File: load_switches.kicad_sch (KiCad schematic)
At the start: 19 parts, among them U10 TPS22965TDSGRQ1, U11 TPS22965TDSGRQ1, U12 TPS22965TDSGRQ1, U9 TPS22965TDSGRQ1

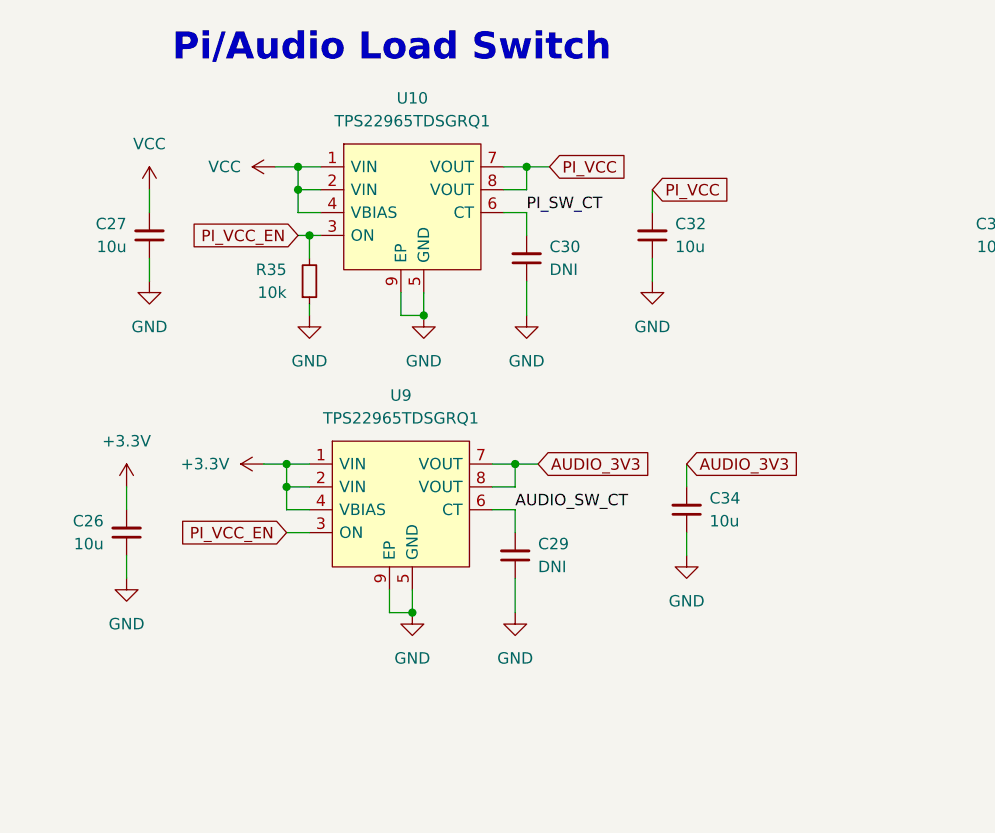
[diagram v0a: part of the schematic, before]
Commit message: schematic: add resistors to allow latching pi power
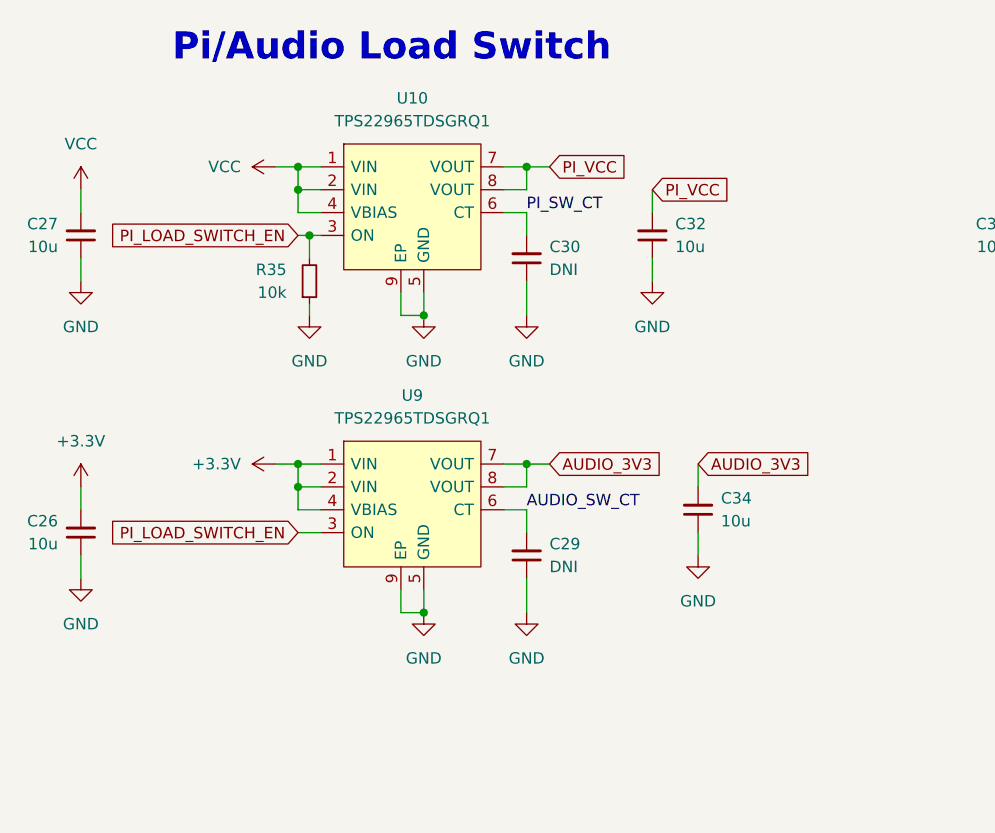
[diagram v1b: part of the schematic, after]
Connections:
- net PI_VCC_EN renamed PI_LOAD_SWITCH_EN
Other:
- moved on the sheet: C26, C27, C29, C34, U9

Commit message: ci: prepare files for CI
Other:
- title: (none) -> piPod IO/SMC Board
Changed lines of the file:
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@@
 (kicad_sch (version 20211123) (generator eeschema)
   (paper "A4")
+  (title_block
+    (title "piPod IO/SMC Board")
+    (date "${DATE}")
+    (rev "%{TAG} (${REVISION})")
+  )
   (junction (at 62.23 55.88) (diameter 0) (color 0 0 0 0)
   )

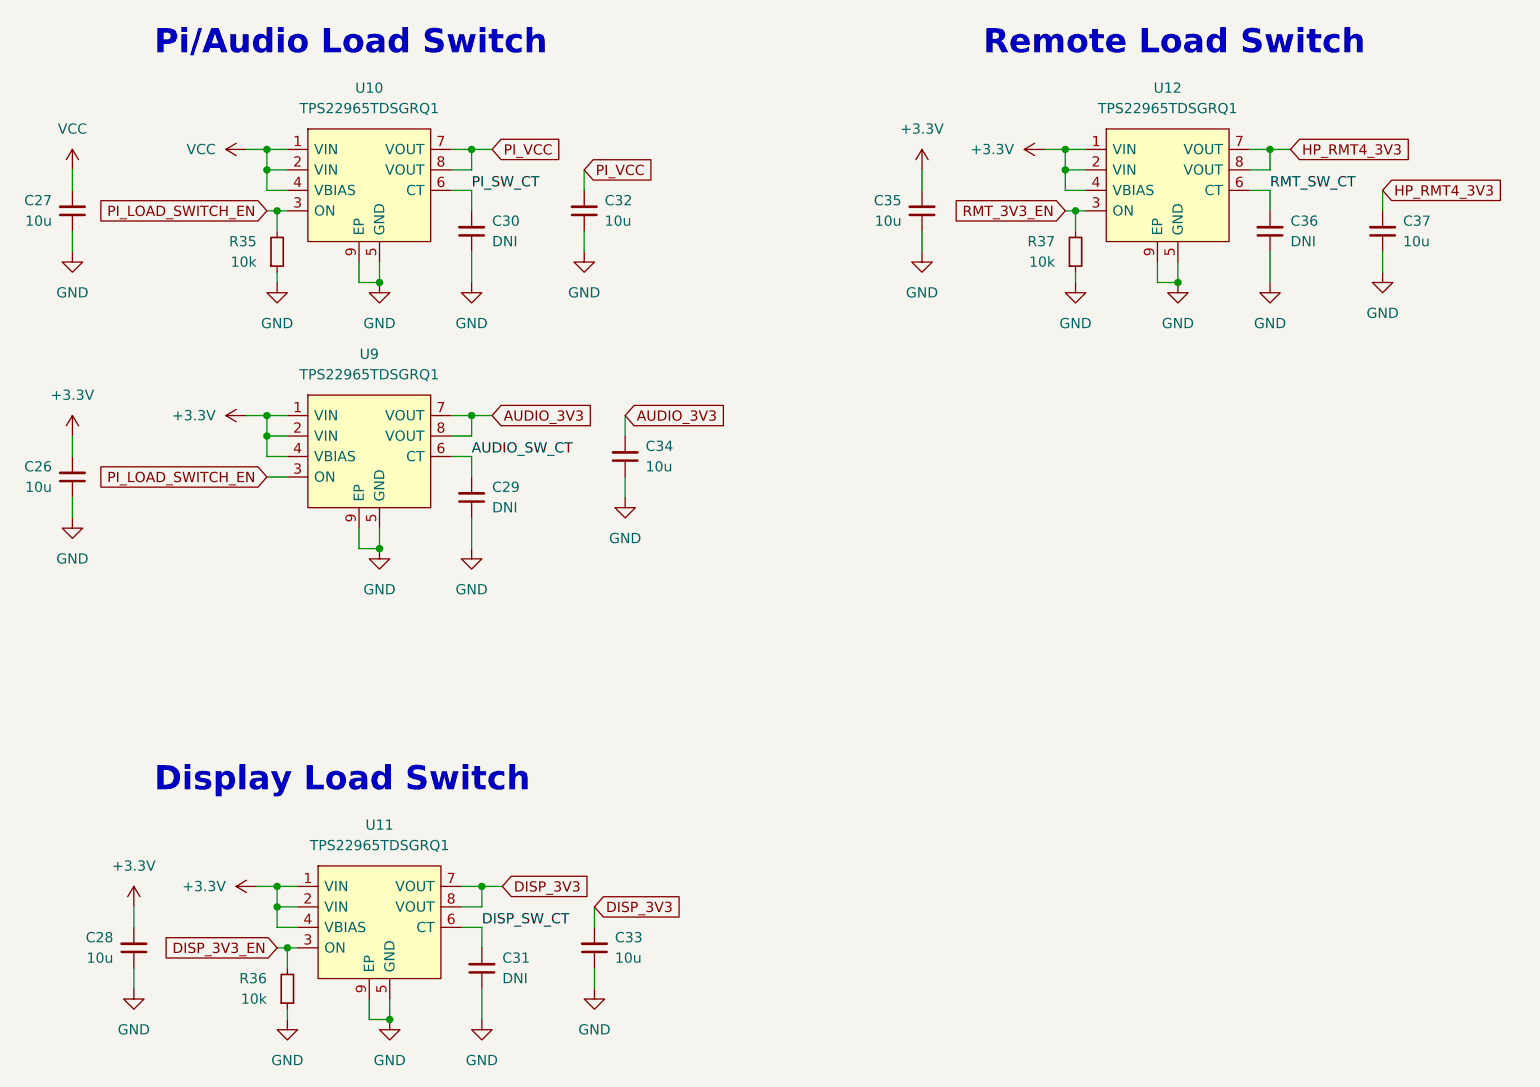
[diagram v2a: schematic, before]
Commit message: ci: test marking parts in sch for bom
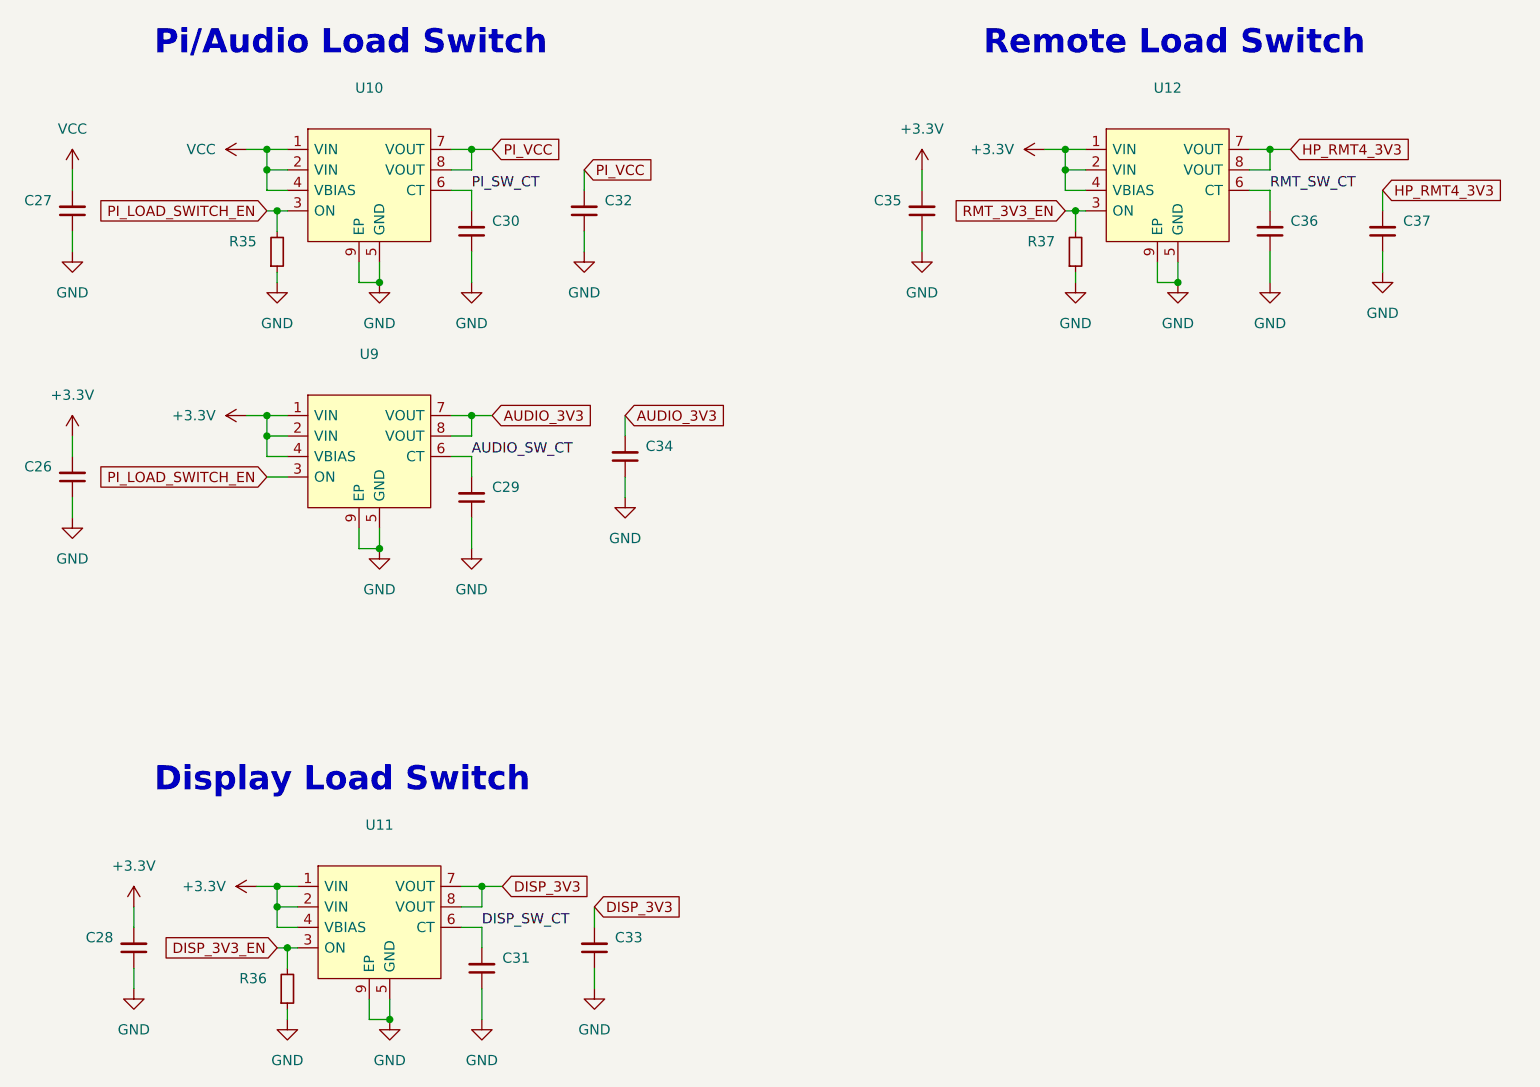
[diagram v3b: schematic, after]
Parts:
- C26, C27, C28, C32, C33, C34, C35, C37: value 10u -> (none); footprint Capacitor_SMD:C_0402_1005Metric -> (none)
- C29: value DNI -> (none); footprint Capacitor_SMD:C_0402_1005Metric -> (none); now left out of the parts list
- C30, C31, C36: value DNI -> (none); footprint Capacitor_SMD:C_0402_1005Metric -> (none)
- R35, R36, R37: value 10k -> (none); footprint Resistor_SMD:R_0402_1005Metric -> (none)
- U10, U11, U12, U9: value TPS22965TDSGRQ1 -> (none); footprint Package_SON:WSON-8-1EP_2x2mm_P0.5mm_EP0.9x1.6mm -> (none)
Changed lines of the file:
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@@
       (effects (font (size 1.27 1.27)) (justify right))
     )
-    (property "Value" "10u" (id 1) (at 95.25 78.7335 0)
-      (effects (font (size 1.27 1.27)) (justify right))
-    )
-    (property "Footprint" "Capacitor_SMD:C_0402_1005Metric" (id 2) (at 92.71 77.47 0)
+    (property "Value" "" (id 1) (at 95.25 78.7335 0)
+      (effects (font (size 1.27 1.27)) (justify right))
+    )
+    (property "Footprint" "" (id 2) (at 92.71 77.47 0)
       (effects (font (size 1.27 1.27)) hide)
     )
@@
       (effects (font (size 1.27 1.27)) (justify right))
     )
-    (property "Value" "10u" (id 1) (at 21.59 81.2735 0)
-      (effects (font (size 1.27 1.27)) (justify right))
-    )
-    (property "Footprint" "Capacitor_SMD:C_0402_1005Metric" (id 2) (at 24.13 80.01 0)
+    (property "Value" "" (id 1) (at 21.59 81.2735 0)
+      (effects (font (size 1.27 1.27)) (justify right))
+    )
+    (property "Footprint" "" (id 2) (at 24.13 80.01 0)
       (effects (font (size 1.27 1.27)) hide)
     )
@@
       (effects (font (size 1.27 1.27)) (justify right))
     )
-    (property "Value" "DNI" (id 1) (at 76.2 50.7935 0)
-      (effects (font (size 1.27 1.27)) (justify right))
-    )
-    (property "Footprint" "Capacitor_SMD:C_0402_1005Metric" (id 2) (at 73.66 49.53 0)
+    (property "Value" "" (id 1) (at 76.2 50.7935 0)
+      (effects (font (size 1.27 1.27)) (justify right))
+    )
+    (property "Footprint" "" (id 2) (at 73.66 49.53 0)
       (effects (font (size 1.27 1.27)) hide)
     )
@@
       (effects (font (size 1.27 1.27)) (justify right))
     )
-    (property "Value" "DNI" (id 1) (at 77.47 142.2335 0)
-      (effects (font (size 1.27 1.27)) (justify right))
-    )
-    (property "Footprint" "Capacitor_SMD:C_0402_1005Metric" (id 2) (at 74.93 140.97 0)
+    (property "Value" "" (id 1) (at 77.47 142.2335 0)
+      (effects (font (size 1.27 1.27)) (justify right))
+    )
+    (property "Footprint" "" (id 2) (at 74.93 140.97 0)
       (effects (font (size 1.27 1.27)) hide)
     )
@@
       (effects (font (size 1.27 1.27)) (justify right))
     )
-    (property "Value" "10u" (id 1) (at 91.44 139.6935 0)
-      (effects (font (size 1.27 1.27)) (justify right))
-    )
-    (property "Footprint" "Capacitor_SMD:C_0402_1005Metric" (id 2) (at 88.9 138.43 0)
+    (property "Value" "" (id 1) (at 91.44 139.6935 0)
+      (effects (font (size 1.27 1.27)) (justify right))
+    )
+    (property "Footprint" "" (id 2) (at 88.9 138.43 0)
       (effects (font (size 1.27 1.27)) hide)
     )
@@
   )
   (symbol (lib_id "Device:C_Small") (at 73.66 82.55 180) (unit 1)
-    (in_bom yes) (on_board yes) (fields_autoplaced)
+    (in_bom no) (on_board yes) (fields_autoplaced)
     (property "Reference" "C29" (id 0) (at 76.2 81.2735 0)
       (effects (font (size 1.27 1.27)) (justify right))
     )
-    (property "Value" "DNI" (id 1) (at 76.2 83.8135 0)
-      (effects (font (size 1.27 1.27)) (justify right))
-    )
-    (property "Footprint" "Capacitor_SMD:C_0402_1005Metric" (id 2) (at 73.66 82.55 0)
+    (property "Value" "" (id 1) (at 76.2 83.8135 0)
+      (effects (font (size 1.27 1.27)) (justify right))
+    )
+    (property "Footprint" "" (id 2) (at 73.66 82.55 0)
       (effects (font (size 1.27 1.27)) hide)
     )
@@
       (effects (font (size 1.27 1.27)) (justify right))
     )
-    (property "Value" "10u" (id 1) (at 90.17 48.2535 0)
-      (effects (font (size 1.27 1.27)) (justify right))
-    )
-    (property "Footprint" "Capacitor_SMD:C_0402_1005Metric" (id 2) (at 87.63 46.99 0)
+    (property "Value" "" (id 1) (at 90.17 48.2535 0)
+      (effects (font (size 1.27 1.27)) (justify right))
+    )
+    (property "Footprint" "" (id 2) (at 87.63 46.99 0)
       (effects (font (size 1.27 1.27)) hide)
     )
@@
       (effects (font (size 1.27 1.27)) (justify right))
     )
-    (property "Value" "10k" (id 1) (at 146.05 53.3399 0)
-      (effects (font (size 1.27 1.27)) (justify right))
-    )
-    (property "Footprint" "Resistor_SMD:R_0402_1005Metric" (id 2) (at 148.59 52.07 0)
+    (property "Value" "" (id 1) (at 146.05 53.3399 0)
+      (effects (font (size 1.27 1.27)) (justify right))
+    )
+    (property "Footprint" "" (id 2) (at 148.59 52.07 0)
       (effects (font (size 1.27 1.27)) hide)
     )
@@
       (effects (font (size 1.27 1.27)) (justify right))
     )
-    (property "Value" "10k" (id 1) (at 48.26 144.7799 0)
-      (effects (font (size 1.27 1.27)) (justify right))
-    )
-    (property "Footprint" "Resistor_SMD:R_0402_1005Metric" (id 2) (at 50.8 143.51 0)
+    (property "Value" "" (id 1) (at 48.26 144.7799 0)
+      (effects (font (size 1.27 1.27)) (justify right))
+    )
+    (property "Footprint" "" (id 2) (at 50.8 143.51 0)
       (effects (font (size 1.27 1.27)) hide)
     )
@@
       (effects (font (size 1.27 1.27)) (justify right))
     )
-    (property "Value" "10k" (id 1) (at 46.99 53.3399 0)
-      (effects (font (size 1.27 1.27)) (justify right))
-    )
-    (property "Footprint" "Resistor_SMD:R_0402_1005Metric" (id 2) (at 49.53 52.07 0)
+    (property "Value" "" (id 1) (at 46.99 53.3399 0)
+      (effects (font (size 1.27 1.27)) (justify right))
+    )
+    (property "Footprint" "" (id 2) (at 49.53 52.07 0)
       (effects (font (size 1.27 1.27)) hide)
     )
@@
       (effects (font (size 1.27 1.27)) (justify right))
     )
-    (property "Value" "10u" (id 1) (at 189.23 50.7935 0)
-      (effects (font (size 1.27 1.27)) (justify right))
-    )
-    (property "Footprint" "Capacitor_SMD:C_0402_1005Metric" (id 2) (at 186.69 49.53 0)
+    (property "Value" "" (id 1) (at 189.23 50.7935 0)
+      (effects (font (size 1.27 1.27)) (justify right))
+    )
+    (property "Footprint" "" (id 2) (at 186.69 49.53 0)
       (effects (font (size 1.27 1.27)) hide)
     )
@@
       (effects (font (size 1.27 1.27)) (justify right))
     )
-    (property "Value" "10u" (id 1) (at 29.21 139.6935 0)
-      (effects (font (size 1.27 1.27)) (justify right))
-    )
-    (property "Footprint" "Capacitor_SMD:C_0402_1005Metric" (id 2) (at 31.75 138.43 0)
+    (property "Value" "" (id 1) (at 29.21 139.6935 0)
+      (effects (font (size 1.27 1.27)) (justify right))
+    )
+    (property "Footprint" "" (id 2) (at 31.75 138.43 0)
       (effects (font (size 1.27 1.27)) hide)
     )
@@
     (in_bom yes) (on_board yes) (fields_autoplaced)
     (property "Reference" "U10" (id 0) (at 60.96 31.75 0))
-    (property "Value" "TPS22965TDSGRQ1" (id 1) (at 60.96 34.29 0))
-    (property "Footprint" "Package_SON:WSON-8-1EP_2x2mm_P0.5mm_EP0.9x1.6mm" (id 2) (at 43.18 26.67 0)
+    (property "Value" "" (id 1) (at 60.96 34.29 0))
+    (property "Footprint" "" (id 2) (at 43.18 26.67 0)
       (effects (font (size 1.27 1.27)) (justify left) hide)
     )
@@
     (in_bom yes) (on_board yes) (fields_autoplaced)
     (property "Reference" "U12" (id 0) (at 160.02 31.75 0))
-    (property "Value" "TPS22965TDSGRQ1" (id 1) (at 160.02 34.29 0))
-    (property "Footprint" "Package_SON:WSON-8-1EP_2x2mm_P0.5mm_EP0.9x1.6mm" (id 2) (at 142.24 26.67 0)
+    (property "Value" "" (id 1) (at 160.02 34.29 0))
+    (property "Footprint" "" (id 2) (at 142.24 26.67 0)
       (effects (font (size 1.27 1.27)) (justify left) hide)
     )
@@
       (effects (font (size 1.27 1.27)) (justify right))
     )
-    (property "Value" "10u" (id 1) (at 21.59 48.2535 0)
-      (effects (font (size 1.27 1.27)) (justify right))
-    )
-    (property "Footprint" "Capacitor_SMD:C_0402_1005Metric" (id 2) (at 24.13 46.99 0)
+    (property "Value" "" (id 1) (at 21.59 48.2535 0)
+      (effects (font (size 1.27 1.27)) (justify right))
+    )
+    (property "Footprint" "" (id 2) (at 24.13 46.99 0)
       (effects (font (size 1.27 1.27)) hide)
     )
@@
     (in_bom yes) (on_board yes) (fields_autoplaced)
     (property "Reference" "U9" (id 0) (at 60.96 64.77 0))
-    (property "Value" "TPS22965TDSGRQ1" (id 1) (at 60.96 67.31 0))
-    (property "Footprint" "Package_SON:WSON-8-1EP_2x2mm_P0.5mm_EP0.9x1.6mm" (id 2) (at 43.18 59.69 0)
+    (property "Value" "" (id 1) (at 60.96 67.31 0))
+    (property "Footprint" "" (id 2) (at 43.18 59.69 0)
       (effects (font (size 1.27 1.27)) (justify left) hide)
     )
@@
       (effects (font (size 1.27 1.27)) (justify right))
     )
-    (property "Value" "DNI" (id 1) (at 175.26 50.7935 0)
-      (effects (font (size 1.27 1.27)) (justify right))
-    )
-    (property "Footprint" "Capacitor_SMD:C_0402_1005Metric" (id 2) (at 172.72 49.53 0)
+    (property "Value" "" (id 1) (at 175.26 50.7935 0)
+      (effects (font (size 1.27 1.27)) (justify right))
+    )
+    (property "Footprint" "" (id 2) (at 172.72 49.53 0)
       (effects (font (size 1.27 1.27)) hide)
     )
@@
       (effects (font (size 1.27 1.27)) (justify right))
     )
-    (property "Value" "10u" (id 1) (at 127 48.2535 0)
-      (effects (font (size 1.27 1.27)) (justify right))
-    )
-    (property "Footprint" "Capacitor_SMD:C_0402_1005Metric" (id 2) (at 129.54 46.99 0)
+    (property "Value" "" (id 1) (at 127 48.2535 0)
+      (effects (font (size 1.27 1.27)) (justify right))
+    )
+    (property "Footprint" "" (id 2) (at 129.54 46.99 0)
       (effects (font (size 1.27 1.27)) hide)
     )
@@
     (in_bom yes) (on_board yes) (fields_autoplaced)
     (property "Reference" "U11" (id 0) (at 62.23 123.19 0))
-    (property "Value" "TPS22965TDSGRQ1" (id 1) (at 62.23 125.73 0))
-    (property "Footprint" "Package_SON:WSON-8-1EP_2x2mm_P0.5mm_EP0.9x1.6mm" (id 2) (at 44.45 118.11 0)
-      (effects (font (size 1.27 1.27)) (justify left) hide)
-    )
+    (property "Value" "" (id 1) (at 62.23 125.73 0))
+    (property "Footprint" "" (id 2) (at 44.45 118.11 0)
+      (effects (font (size 1.27 1.27)) (justify left) hide)
+    )

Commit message: ci: remove populate column
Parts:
- C29: now in the parts list
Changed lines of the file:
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@@
   )
   (symbol (lib_id "Device:C_Small") (at 73.66 82.55 180) (unit 1)
-    (in_bom no) (on_board yes) (fields_autoplaced)
+    (in_bom yes) (on_board yes) (fields_autoplaced)
     (property "Reference" "C29" (id 0) (at 76.2 81.2735 0)
       (effects (font (size 1.27 1.27)) (justify right))
